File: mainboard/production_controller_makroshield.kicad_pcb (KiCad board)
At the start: 2 copper layers, 175.3 x 177.8 mm, 61 parts, among them J1 CON_TERM_BLK_1X2_TB008A-508-0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, J10 CON_CONNAXIO_MOTOR_DRIVER, J11 CON_CONNAXIO_MOTOR_DRIVER, J12 CON_CONNAXIO_MOTOR_DRIVER, J13 CON_CONNAXIO_MOTOR_DRIVER, J14 CON_CONNAXIO_MOTOR_DRIVER, J15 CON_CONNAXIO_MOTOR_DRIVER, J16 CON_CONNAXIO_MOTOR_DRIVER, J17 CON_CONNAXIO_MOTOR_DRIVER, J18 CON_CONNAXIO_MOTOR_DRIVER, J19 CON_CONNAXIO_MOTOR_DRIVER, J2 CON_HDR_MIKROBUS_ADDON_TH, J3 CON_HDR_MIKROBUS_SOCKET_TH, J4 CON_CONNAXIO_MOTOR_DRIVER, J5 CON_CONNAXIO_MOTOR_DRIVER, J6 CON_CONNAXIO_MOTOR_DRIVER, J7 CON_CONNAXIO_MOTOR_DRIVER, J8 CON_CONNAXIO_MOTOR_DRIVER, J9 CON_CONNAXIO_MOTOR_DRIVER, Q1 TRX_PMOS_AOD4189, Q2 TRX_NPN_MMBT3904-TP, U1 IO_EXP_PI4IOE5V6416ZDEX, U2 IO_EXP_PI4IOE5V6416ZDEX, U3 CON_BARREL_2.1X5.5_PJ-002A, U4 SUN_CUR_ACS711KEXLT-31AB-T, U5 ADC_NAU7802SGI

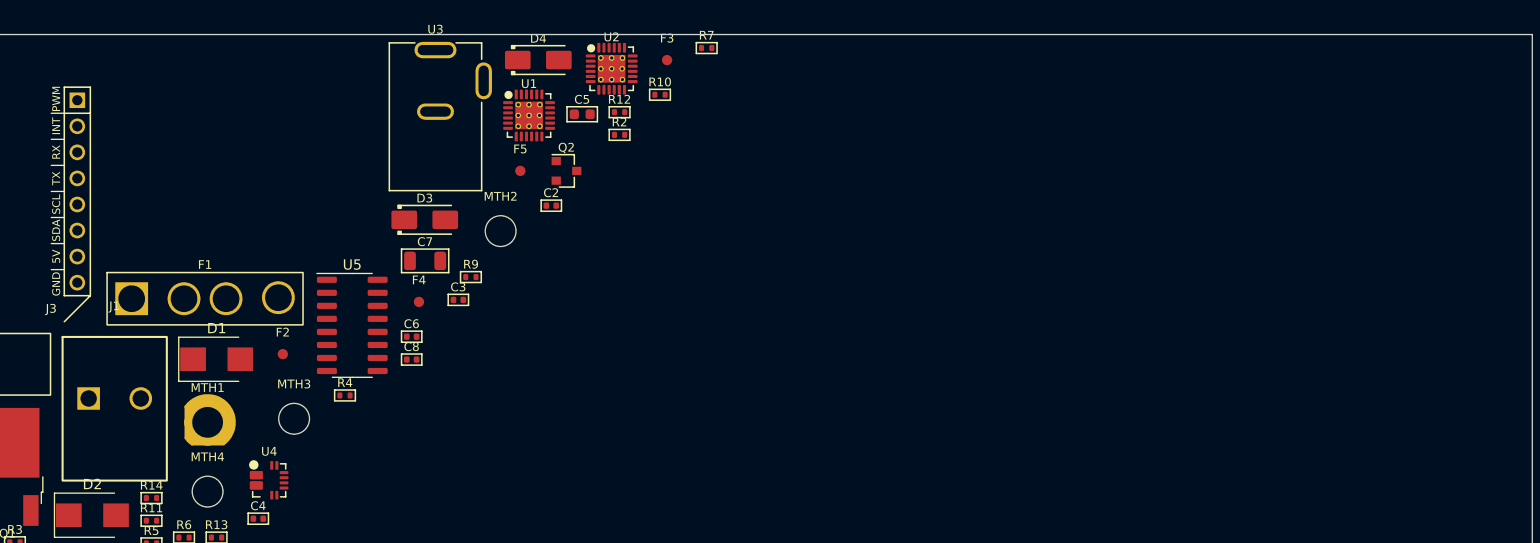
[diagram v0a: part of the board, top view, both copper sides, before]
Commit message: rename project, comple simple switch layout, fix thermal reliefs
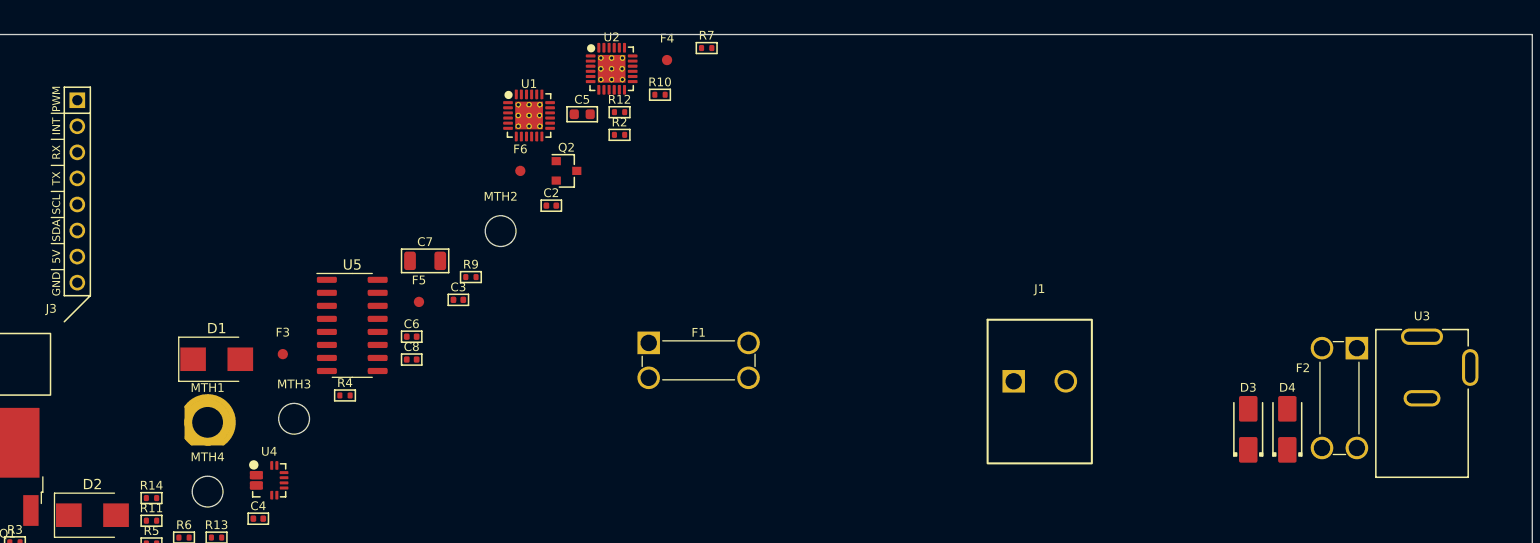
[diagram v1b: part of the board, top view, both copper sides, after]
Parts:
- added F2: FUS_BLADE_MINI_3588-1, connaxio-connectors:FUS_BLADE_MINI_3588-1, F.Cu at (171.3, 53.2)
- F1: value FUS_BLADE_3522 -> FUS_BLADE_MINI_3588-1; footprint connaxio-connectors:FUS_BLADE_3522 -> connaxio-connectors:FUS_BLADE_MINI_3588-1
- moved U3 100.1 mm to (179.4, 53.7)
- moved J1 90.2 mm to (142.1, 51.6)
- moved D3 82.8 mm to (162.4, 56.3), turned to 90 degrees
- moved D4 81.4 mm to (166.2, 56.3), turned to 90 degrees
- moved F1 48.5 mm to (108.9, 49.5)
- renumbered F2 to F3, F3 to F4, F4 to F5, F5 to F6
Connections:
- D3 pad 1: +5V -> Net-(D3-Pad1)
- D3 pad 2: Net-(D3-Pad2) -> +5V
- D4 pad 1: +5V -> Net-(D3-Pad1)
- U3 pad 1: Net-(D3-Pad2) -> Net-(U3-Pad1)

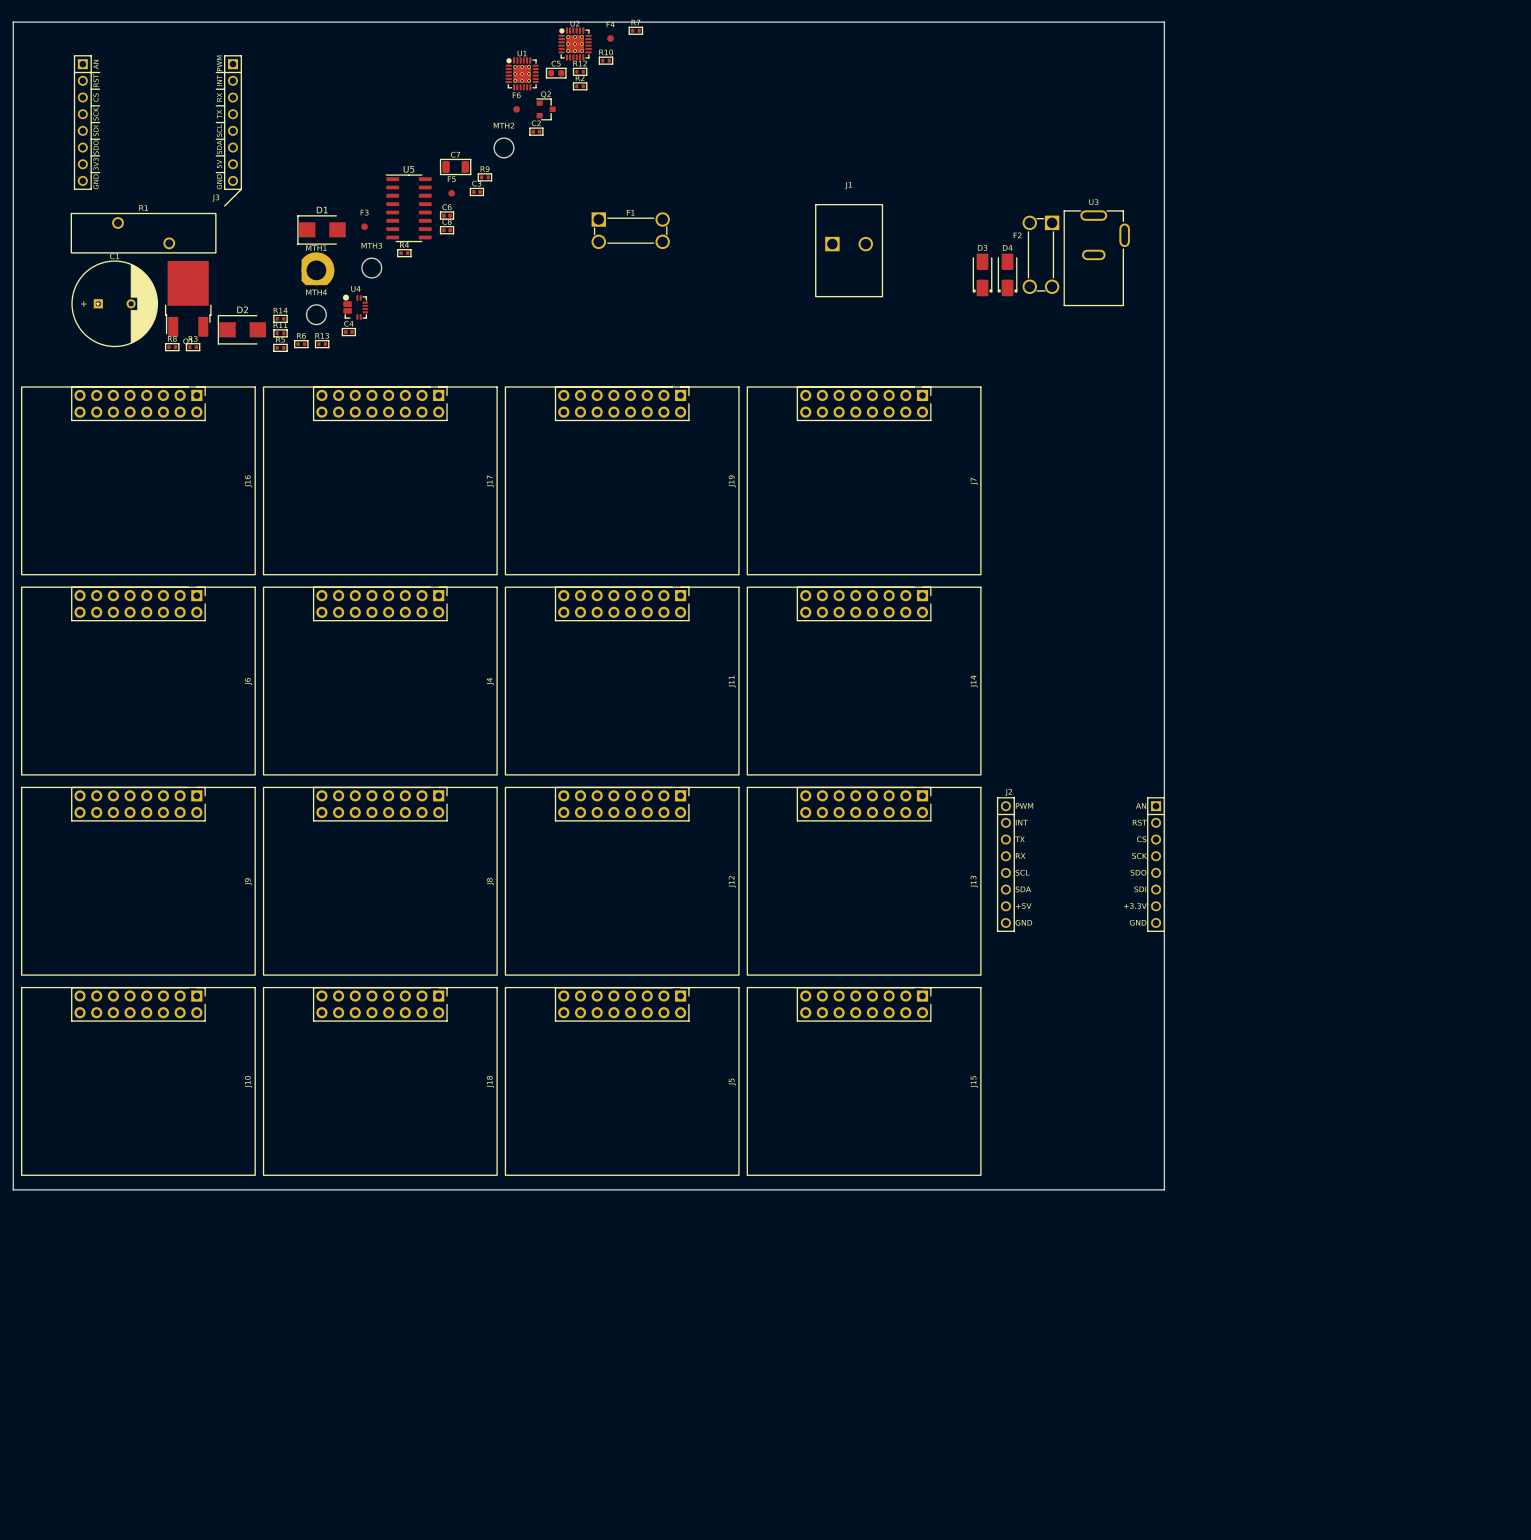
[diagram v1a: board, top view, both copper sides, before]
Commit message: Inverted motor controls for open-drain operation and manual switch override compatibility
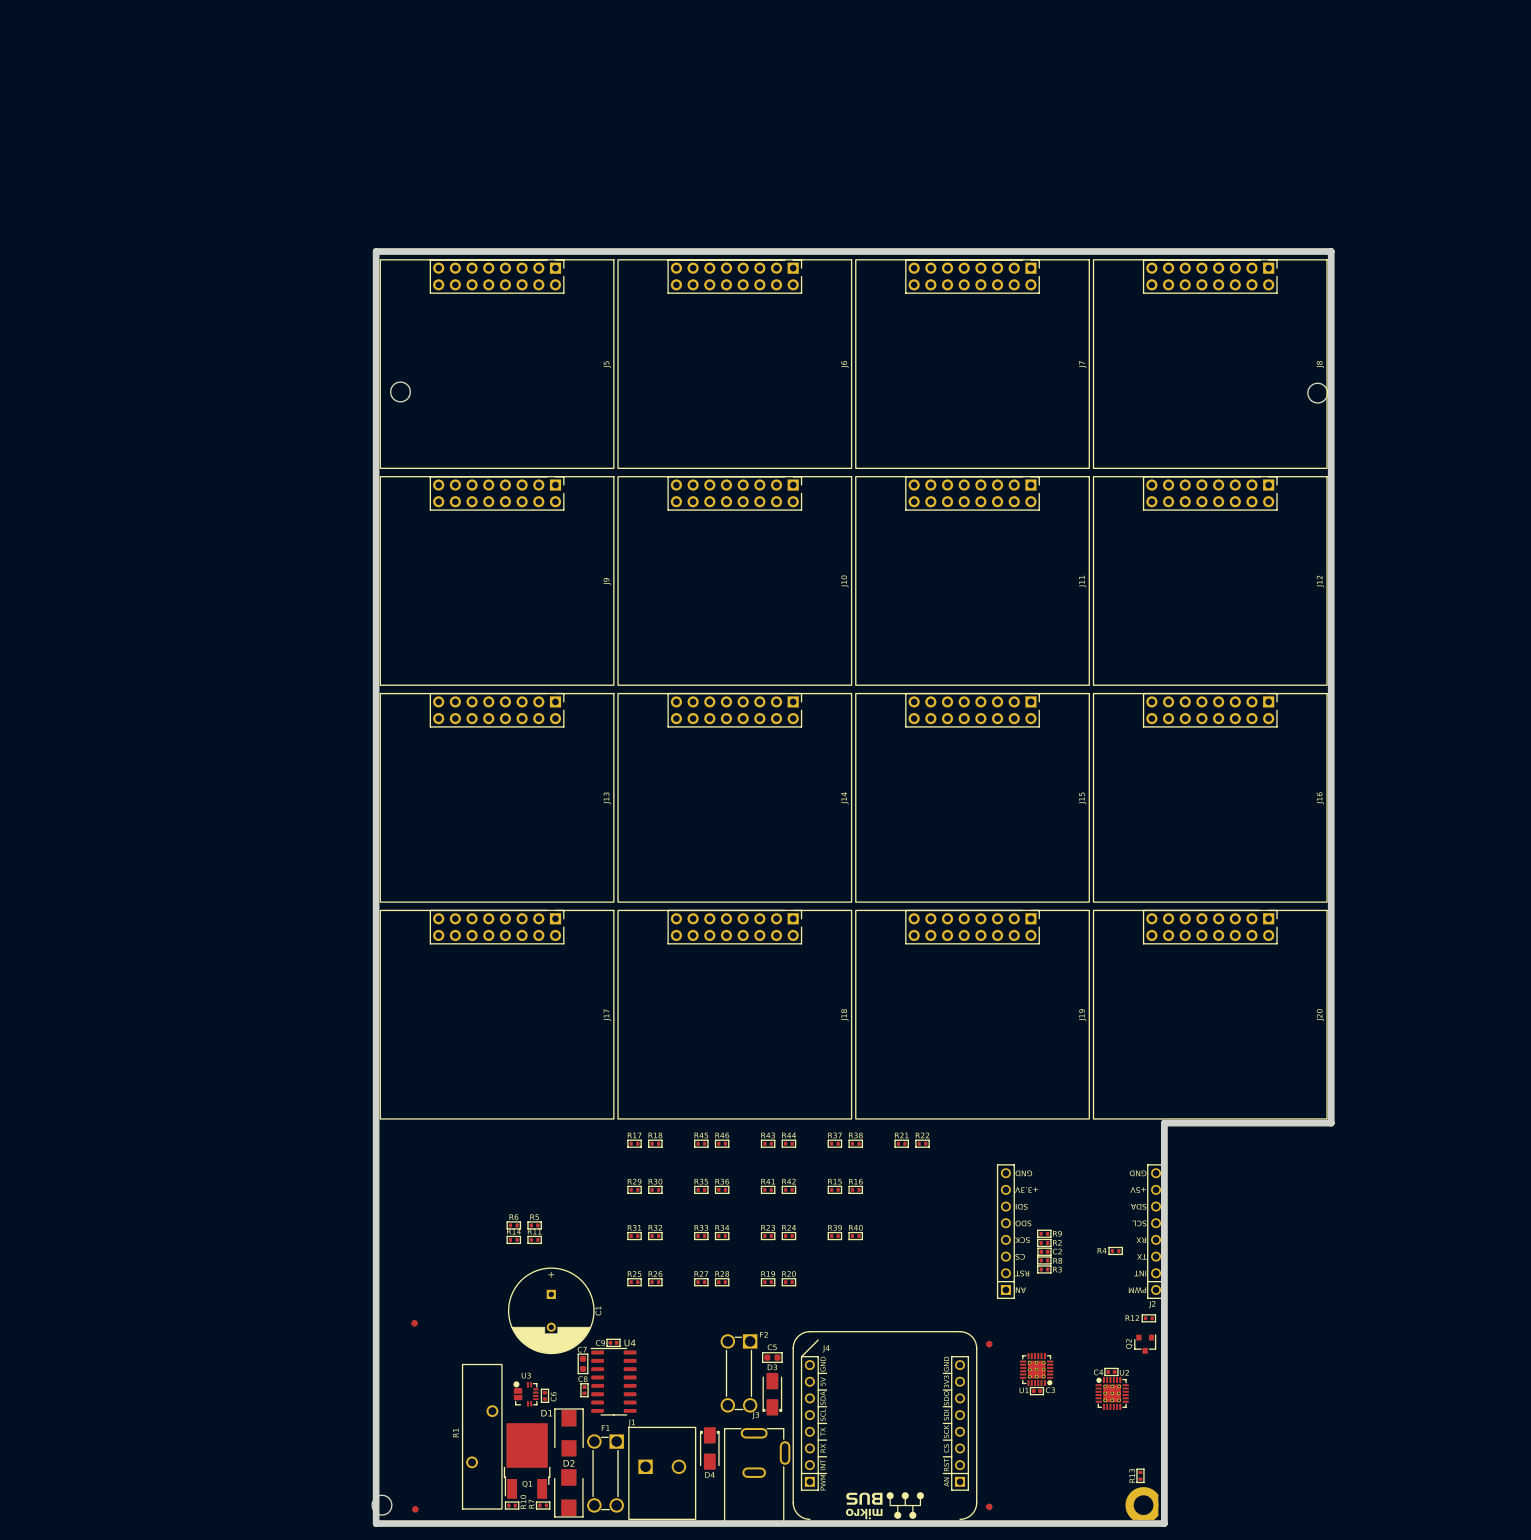
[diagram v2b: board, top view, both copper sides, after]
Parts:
- removed the J5 at (107.6, 179.1)
- added C9: CAP_CER_100NF_25V_0402, connaxio-capacitors:CAP_CER_0402_1005M, F.Cu at (106.2, 218.9)
- added J20: CON_CONNAXIO_MOTOR_DRIVER, connaxio-connectors:CON_CONNAXIO_MOTOR_DRIVER, F.Cu at (197.1, 168.9)
- added R15: RES_12.4KΩ_1%_0402, connaxio-resistors:RES_0402_1005M, F.Cu at (140.0, 195.6)
- added R16: RES_12.4KΩ_1%_0402, connaxio-resistors:RES_0402_1005M, F.Cu at (143.1, 195.6)
- added R17: RES_12.4KΩ_1%_0402, connaxio-resistors:RES_0402_1005M, F.Cu at (109.4, 188.6)
- added R18: RES_12.4KΩ_1%_0402, connaxio-resistors:RES_0402_1005M, F.Cu at (112.6, 188.6)
- added R19: RES_12.4KΩ_1%_0402, connaxio-resistors:RES_0402_1005M, F.Cu at (129.8, 209.6)
- added R20: RES_12.4KΩ_1%_0402, connaxio-resistors:RES_0402_1005M, F.Cu at (133.0, 209.6)
- added R21: RES_12.4KΩ_1%_0402, connaxio-resistors:RES_0402_1005M, F.Cu at (150.1, 188.6)
- added R22: RES_12.4KΩ_1%_0402, connaxio-resistors:RES_0402_1005M, F.Cu at (153.3, 188.6)
- added R23: RES_12.4KΩ_1%_0402, connaxio-resistors:RES_0402_1005M, F.Cu at (129.8, 202.6)
- added R24: RES_12.4KΩ_1%_0402, connaxio-resistors:RES_0402_1005M, F.Cu at (133.0, 202.6)
- added R25: RES_12.4KΩ_1%_0402, connaxio-resistors:RES_0402_1005M, F.Cu at (109.4, 209.6)
- added R26: RES_12.4KΩ_1%_0402, connaxio-resistors:RES_0402_1005M, F.Cu at (112.6, 209.6)
- added R27: RES_12.4KΩ_1%_0402, connaxio-resistors:RES_0402_1005M, F.Cu at (119.6, 209.6)
- added R28: RES_12.4KΩ_1%_0402, connaxio-resistors:RES_0402_1005M, F.Cu at (122.8, 209.6)
- added R29: RES_12.4KΩ_1%_0402, connaxio-resistors:RES_0402_1005M, F.Cu at (109.4, 195.6)
- added R30: RES_12.4KΩ_1%_0402, connaxio-resistors:RES_0402_1005M, F.Cu at (112.6, 195.6)
- added R31: RES_12.4KΩ_1%_0402, connaxio-resistors:RES_0402_1005M, F.Cu at (109.4, 202.6)
- added R32: RES_12.4KΩ_1%_0402, connaxio-resistors:RES_0402_1005M, F.Cu at (112.6, 202.6)
- added R33: RES_12.4KΩ_1%_0402, connaxio-resistors:RES_0402_1005M, F.Cu at (119.6, 202.6)
- added R34: RES_12.4KΩ_1%_0402, connaxio-resistors:RES_0402_1005M, F.Cu at (122.8, 202.6)
- added R35: RES_12.4KΩ_1%_0402, connaxio-resistors:RES_0402_1005M, F.Cu at (119.6, 195.6)
- added R36: RES_12.4KΩ_1%_0402, connaxio-resistors:RES_0402_1005M, F.Cu at (122.8, 195.6)
- added R37: RES_12.4KΩ_1%_0402, connaxio-resistors:RES_0402_1005M, F.Cu at (140.0, 188.6)
- added R38: RES_12.4KΩ_1%_0402, connaxio-resistors:RES_0402_1005M, F.Cu at (143.1, 188.6)
- added R39: RES_12.4KΩ_1%_0402, connaxio-resistors:RES_0402_1005M, F.Cu at (140.0, 202.6)
- added R40: RES_12.4KΩ_1%_0402, connaxio-resistors:RES_0402_1005M, F.Cu at (143.1, 202.6)
- added R41: RES_12.4KΩ_1%_0402, connaxio-resistors:RES_0402_1005M, F.Cu at (129.8, 195.6)
- added R42: RES_12.4KΩ_1%_0402, connaxio-resistors:RES_0402_1005M, F.Cu at (133.0, 195.6)
- added R43: RES_12.4KΩ_1%_0402, connaxio-resistors:RES_0402_1005M, F.Cu at (129.8, 188.6)
- added R44: RES_12.4KΩ_1%_0402, connaxio-resistors:RES_0402_1005M, F.Cu at (133.0, 188.6)
- added R45: RES_12.4KΩ_1%_0402, connaxio-resistors:RES_0402_1005M, F.Cu at (119.6, 188.6)
- added R46: RES_12.4KΩ_1%_0402, connaxio-resistors:RES_0402_1005M, F.Cu at (122.8, 188.6)
- C7: value CAP_CER_10UF_25V_1206 -> CAP_CER_22UF_10V_0603; footprint connaxio-capacitors:CAP_CER_1206_3216M -> connaxio-capacitors:CAP_CER_0603_1608M
- R11: value RES_1.54KΩ_1%_0402 -> RES_12.4KΩ_1%_0402
- R14: value RES_12.4KΩ_1%_0402 -> RES_5.10KΩ_1%_0402
- R5, R6: value RES_1.54KΩ_1%_0402 -> RES_5.10KΩ_1%_0402
- moved J4 226.9 mm to (147.6, 231.1), turned to 180 degrees
- moved MTH1 226.3 mm to (186.9, 243.6), turned to 90 degrees
- moved R7 225.0 mm to (95.5, 243.6), turned to 180 degrees
- moved U2 221.1 mm to (182.2, 226.6)
- moved R10 220.5 mm to (90.8, 243.6), turned to 180 degrees
- moved F3 216.9 mm to (163.4, 243.8)
- moved R13 212.6 mm to (186.5, 239.1), turned to 90 degrees
- moved U1 212.3 mm to (170.7, 222.9), turned to 180 degrees
- moved Q2 209.0 mm to (187.2, 219.1), turned to -90 degrees
- moved R12 208.6 mm to (187.8, 215.1)
- moved F4 207.0 mm to (163.4, 219.1)
- moved C3 201.5 mm to (170.7, 226.2)
- moved F5 200.5 mm to (76.1, 244.2)
- moved C5 198.3 mm to (130.4, 221.1)
- moved C4 196.3 mm to (182.1, 223.3), turned to 180 degrees
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- renumbered U3 to J3, J3 to J4, J4 to J5, U4 to U3, U5 to U4
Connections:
- D1 pad 1: +24VDC -> /24V_CS
- D1 pad 2: GND -> /24V_Neg
- D2 pad 2: GND -> /24V_Neg
- J10 pad 2: CTRLA7 -> CTRLA6
- J10 pad 4: CTRLB7 -> CTRLB6
- J11 pad 2: CTRLA8 -> CTRLA7
- J11 pad 4: CTRLB8 -> CTRLB7
- J12 pad 2: CTRLA9 -> CTRLA8
- J12 pad 4: CTRLB9 -> CTRLB8
- J13 pad 2: CTRLA10 -> CTRLA9
- J13 pad 4: CTRLB10 -> CTRLB9
- J14 pad 2: CTRLA11 -> CTRLA10
- J14 pad 4: CTRLB11 -> CTRLB10
- J15 pad 2: CTRLA12 -> CTRLA11
- J15 pad 4: CTRLB12 -> CTRLB11
- J16 pad 2: CTRLA13 -> CTRLA12
- J16 pad 4: CTRLB13 -> CTRLB12
- J17 pad 2: CTRLA14 -> CTRLA13
- J17 pad 4: CTRLB14 -> CTRLB13
- J18 pad 2: CTRLA15 -> CTRLA14
- J18 pad 4: CTRLB15 -> CTRLB14
- J19 pad 2: CTRLA16 -> CTRLA15
- J19 pad 4: CTRLB16 -> CTRLB15
- J6 pad 2: CTRLA3 -> CTRLA2
- J6 pad 4: CTRLB3 -> CTRLB2
- J7 pad 2: CTRLA4 -> CTRLA3
- J7 pad 4: CTRLB4 -> CTRLB3
- J8 pad 2: CTRLA5 -> CTRLA4
- J8 pad 4: CTRLB5 -> CTRLB4
- J9 pad 2: CTRLA6 -> CTRLA5
- J9 pad 4: CTRLB6 -> CTRLB5
- Q1 pad 3: +24VDC -> /24V_CS
- R1 pad 2: +24VDC -> /24V_CS
- U3 pad 1: GND -> /24V_CS
- U3 pad 2: GND -> /24V_CS
- U3 pad 3: /24V_Neg -> +24VDC
- U3 pad 4: /24V_Neg -> +24VDC
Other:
- board size 175.3 x 177.8 mm -> 145.4 x 193.7 mm
